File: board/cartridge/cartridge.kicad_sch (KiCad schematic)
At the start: 33 parts, among them J1 TF-115-BCP9, J2 KH-TYPE-C-16P, J3 TC2030-NL, P1 Card Edge, SW1 K3-1410S, SW2 K3-1410S, U1 AMS1117-3.3, U2 STM32G0B0RETx, U4 NAU8814Y, Y1 X322516MLB4SI

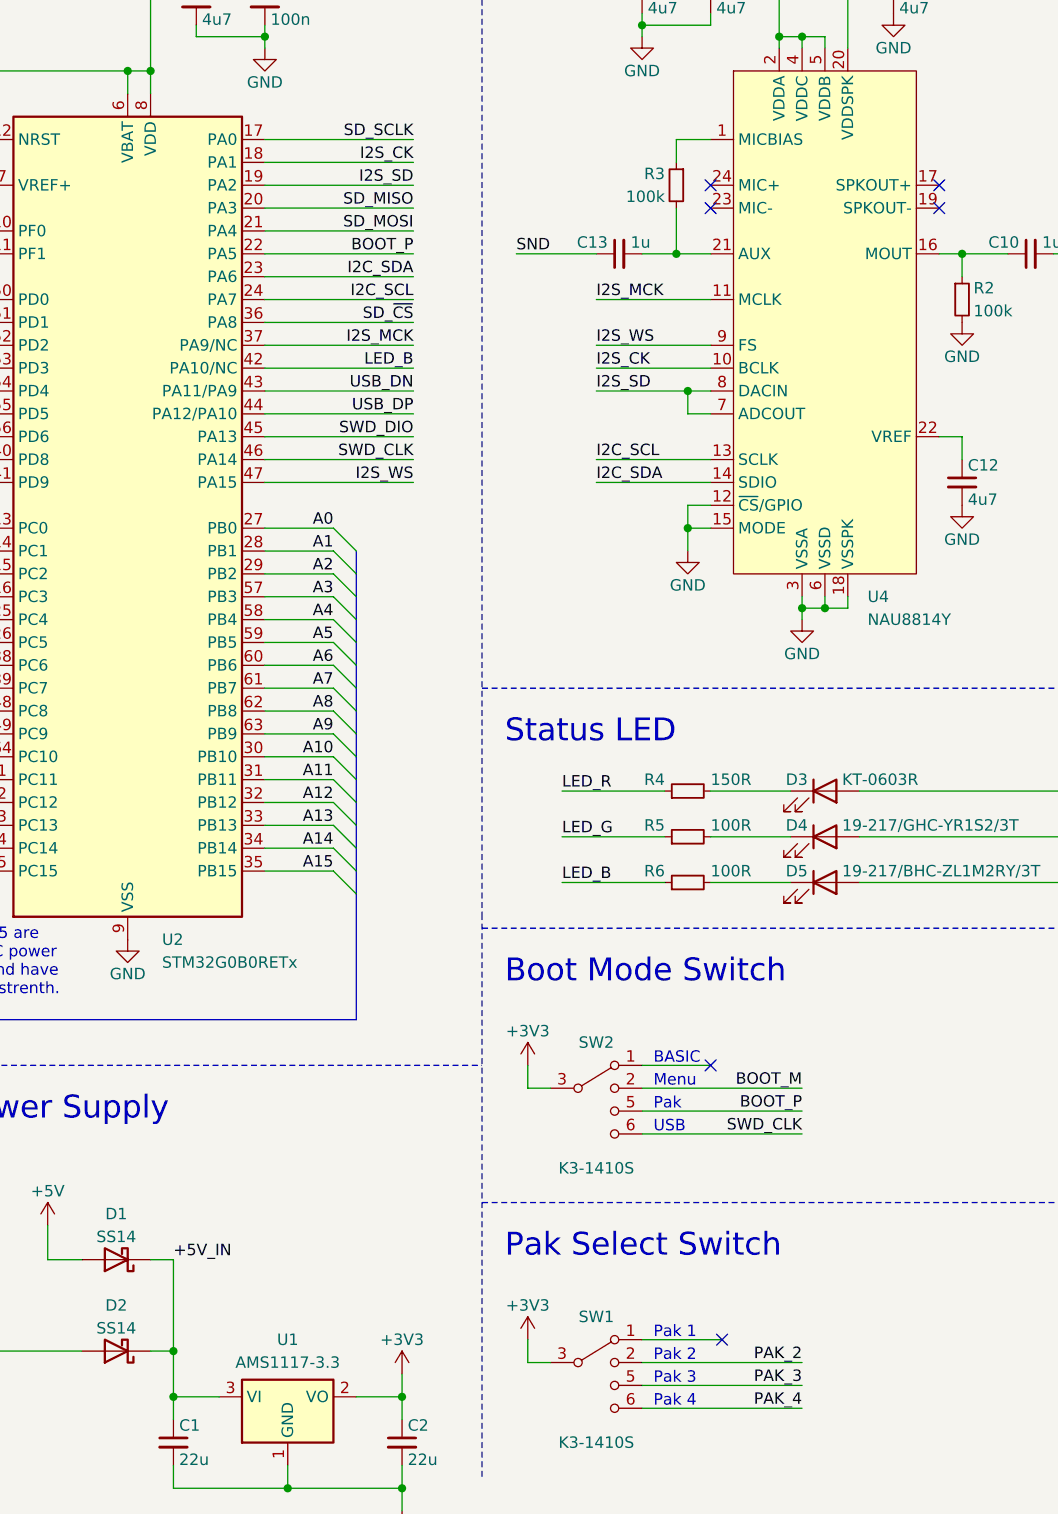
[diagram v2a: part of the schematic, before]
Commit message: Route power for the main ICs.
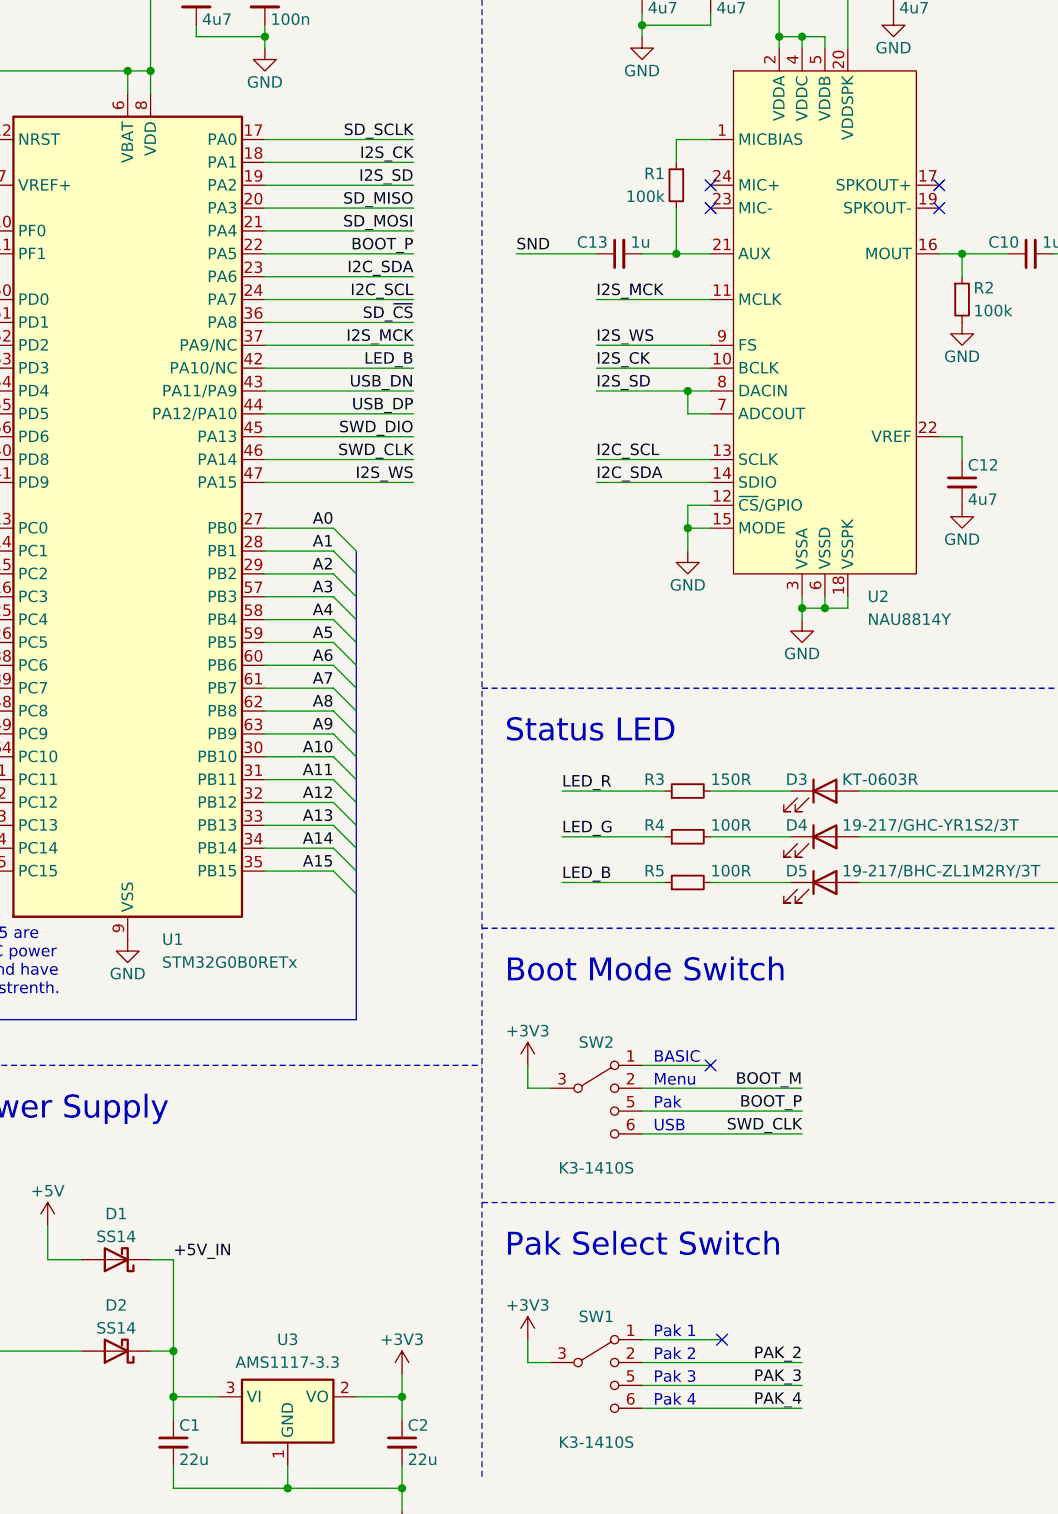
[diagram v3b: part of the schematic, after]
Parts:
- renumbered R3 to R1, R4 to R3, R5 to R4, R6 to R5, U2 to U1, U4 to U2, U1 to U3
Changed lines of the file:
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@@
   (symbol (lib_id "Device:R_Small") (at 215.9 125.73 90) (unit 1)
     (in_bom yes) (on_board yes) (dnp no)
-    (property "Reference" "R6" (at 213.36 124.46 90)
+    (property "Reference" "R5" (at 213.36 124.46 90)
       (effects (font (size 1.27 1.27)) (justify left))
     )
@@
       (project "cartridge"
         (path "/b6472d2e-e93c-4ee2-a887-2e70fff347c6"
-          (reference "R6") (unit 1)
+          (reference "R5") (unit 1)
         )
       )
@@
   (symbol (lib_id "Regulator_Linear:AMS1117-3.3") (at 171.45 182.88 0) (unit 1)
     (in_bom yes) (on_board yes) (dnp no) (fields_autoplaced)
-    (property "Reference" "U1" (at 171.45 176.53 0)
+    (property "Reference" "U3" (at 171.45 176.53 0)
       (effects (font (size 1.27 1.27)))
     )
@@
       (project "cartridge"
         (path "/b6472d2e-e93c-4ee2-a887-2e70fff347c6"
-          (reference "U1") (unit 1)
+          (reference "U3") (unit 1)
         )
       )
@@
   (symbol (lib_id "Device:R_Small") (at 215.9 120.65 90) (unit 1)
     (in_bom yes) (on_board yes) (dnp no)
-    (property "Reference" "R5" (at 213.36 119.38 90)
+    (property "Reference" "R4" (at 213.36 119.38 90)
       (effects (font (size 1.27 1.27)) (justify left))
     )
@@
       (project "cartridge"
         (path "/b6472d2e-e93c-4ee2-a887-2e70fff347c6"
-          (reference "R5") (unit 1)
+          (reference "R4") (unit 1)
         )
       )
@@
   (symbol (lib_id "MCU_ST_STM32G0:STM32G0B0RETx") (at 153.67 86.36 0) (unit 1)
     (in_bom yes) (on_board yes) (dnp no)
-    (property "Reference" "U2" (at 157.48 132.08 0)
+    (property "Reference" "U1" (at 157.48 132.08 0)
       (effects (font (size 1.27 1.27)) (justify left))
     )
@@
       (project "cartridge"
         (path "/b6472d2e-e93c-4ee2-a887-2e70fff347c6"
-          (reference "U2") (unit 1)
+          (reference "U1") (unit 1)
         )
       )
@@
   (symbol (lib_id "Device:R_Small") (at 215.9 115.57 90) (unit 1)
     (in_bom yes) (on_board yes) (dnp no)
-    (property "Reference" "R4" (at 213.36 114.3 90)
+    (property "Reference" "R3" (at 213.36 114.3 90)
       (effects (font (size 1.27 1.27)) (justify left))
     )
@@
       (project "cartridge"
         (path "/b6472d2e-e93c-4ee2-a887-2e70fff347c6"
-          (reference "R4") (unit 1)
+          (reference "R3") (unit 1)
         )
       )
@@
   (symbol (lib_id "Device:R_Small") (at 214.63 48.26 0) (mirror y) (unit 1)
     (in_bom yes) (on_board yes) (dnp no)
-    (property "Reference" "R3" (at 213.36 46.99 0)
+    (property "Reference" "R1" (at 213.36 46.99 0)
       (effects (font (size 1.27 1.27)) (justify left))
     )
@@
       (project "cartridge"
         (path "/b6472d2e-e93c-4ee2-a887-2e70fff347c6"
-          (reference "R3") (unit 1)
+          (reference "R1") (unit 1)
         )
       )
@@
   (symbol (lib_id "0Project:Nuvoton_NAU8814Y") (at 231.14 58.42 0) (unit 1)
     (in_bom yes) (on_board yes) (dnp no) (fields_autoplaced)
-    (property "Reference" "U4" (at 235.8741 93.98 0)
+    (property "Reference" "U2" (at 235.8741 93.98 0)
       (effects (font (size 1.27 1.27)) (justify left))
     )
@@
       (project "cartridge"
         (path "/b6472d2e-e93c-4ee2-a887-2e70fff347c6"
-          (reference "U4") (unit 1)
-        )
-      )
+          (reference "U2") (unit 1)
+        )
+      )

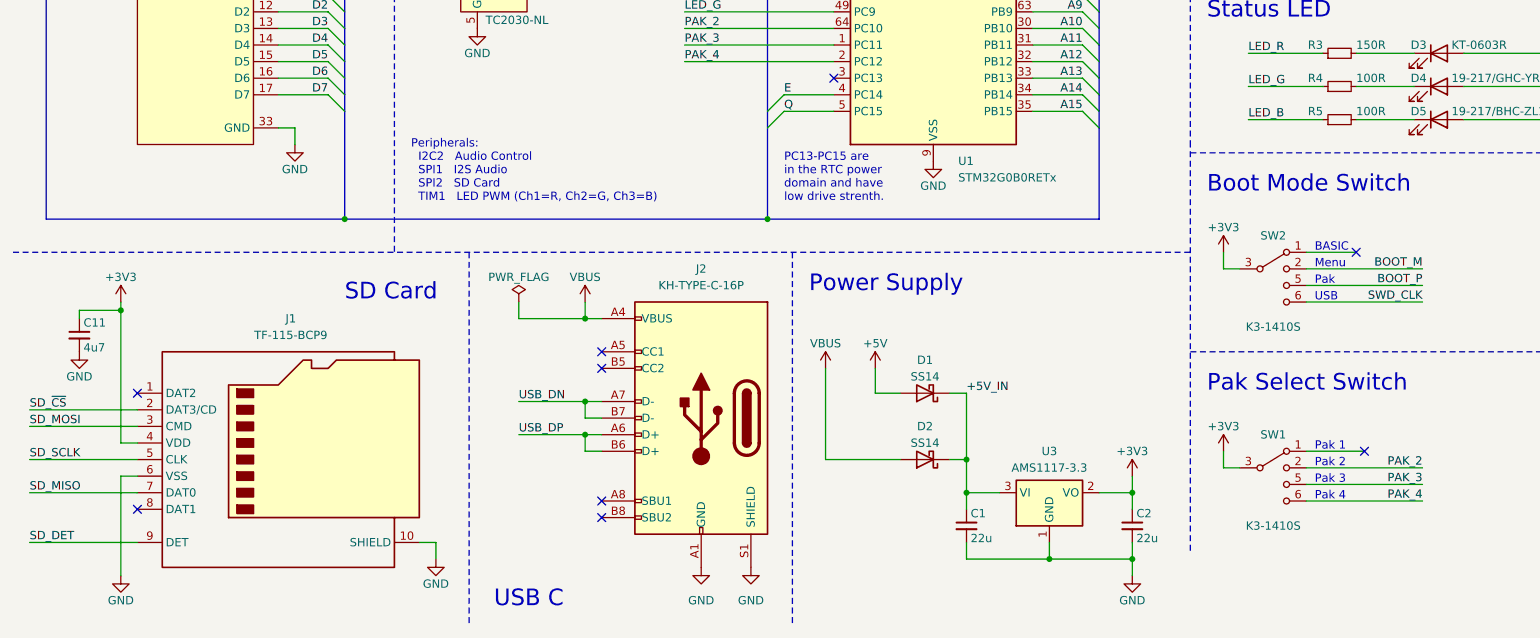
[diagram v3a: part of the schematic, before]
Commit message: Route everything else.
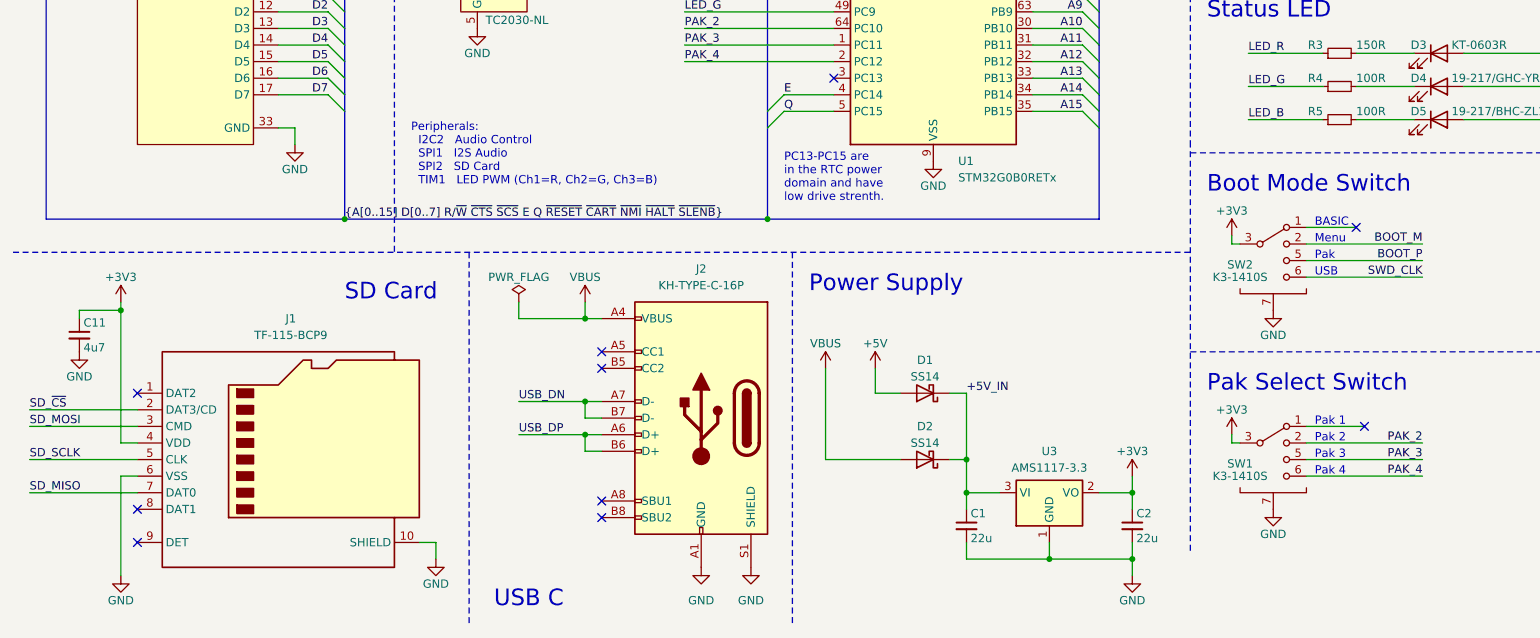
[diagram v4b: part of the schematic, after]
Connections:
- net GND: now also SW1.7 (SHIELD), SW2.7 (SHIELD)
- net SD_DET: no longer names the net of J1.9 (DET)
- no-connect marks 16 -> 17

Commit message: Misc board cleanup.
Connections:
- net VBUS: now also U1.3 (PC13)
- no-connect marks 17 -> 16
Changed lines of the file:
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@@
   (no_connect (at 93.98 106.68))
   (no_connect (at 243.84 48.26))
-  (no_connect (at 138.43 119.38))
   (bus_entry (at 60.96 116.84) (size 2.54 2.54)
     (stroke (width 0) (type default))
@@
     (stroke (width 0) (type default))
   )
+  (wire (pts (xy 109.22 115.57) (xy 109.22 119.38))
+    (stroke (width 0) (type default))
+  )
   (wire (pts (xy 130.81 86.36) (xy 138.43 86.36))
     (stroke (width 0) (type default))
@@
   )
   (wire (pts (xy 22.86 156.21) (xy 22.86 154.94))
+    (stroke (width 0) (type default))
+  )
+  (wire (pts (xy 138.43 119.38) (xy 109.22 119.38))
     (stroke (width 0) (type default))
   )
@@
         )
       )
+    )
+  )
+  (symbol (lib_id "power:VBUS") (at 109.22 115.57 0) (unit 1)
+    (in_bom yes) (on_board yes) (dnp no)
+    (property "Reference" "#PWR033" (at 109.22 119.38 0)
+      (effects (font (size 1.27 1.27)) hide)
+    )
+    (property "Value" "VBUS" (at 109.22 111.76 0)
+      (effects (font (size 1.27 1.27)))
+    )
+    (property "Footprint" "" (at 109.22 115.57 0)
+      (effects (font (size 1.27 1.27)) hide)
+    )
+    (property "Datasheet" "" (at 109.22 115.57 0)
+      (effects (font (size 1.27 1.27)) hide)
+    )
+    (pin "1")
+    (instances
+      (project "cartridge"
+        (path "/b6472d2e-e93c-4ee2-a887-2e70fff347c6"
+          (reference "#PWR033") (unit 1)
+        )
+      )

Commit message: Final cleanup for first cartridge prototype.
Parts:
- J2: value KH-TYPE-C-16P -> HC-TYPE-C-16P-01B; footprint 0Project:KH-TYPE-C-16P -> 0Project:HC-TYPE-C-16P-01B; LCSC C709357 -> C2894898
- R3: value 150R -> 220R
- R4: value 100R -> 120R
- R5: value 100R -> 150R
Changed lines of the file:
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@@
   (title_block
     (title "CoCo Chameleon - Cartridge Emulator")
-    (date "2023-11-24")
+    (date "2023-12-21")
     (rev "v0.1")
     (company "© 2023 Sam Hanes, licensed under CERN-OHL-W v2")
@@
   )
   (text "Peripherals:\n  I2C2   Audio Control\n  SPI1   I2S Audio\n  SPI2   SD Card\n  TIM1   LED PWM (Ch1=R, Ch2=G, Ch3=B)"
-    (at 73.66 135.89 0)
+    (at 73.66 133.35 0)
     (effects (font (size 1.27 1.27)) (justify left bottom))
   )
@@
       (effects (font (size 1.27 1.27)) (justify left))
     )
-    (property "Value" "100R" (at 218.44 124.46 90)
+    (property "Value" "150R" (at 218.44 124.46 90)
       (effects (font (size 1.27 1.27)) (justify right))
     )
@@
       (effects (font (size 1.27 1.27)) (justify left))
     )
-    (property "Value" "100R" (at 218.44 119.38 90)
+    (property "Value" "120R" (at 218.44 119.38 90)
       (effects (font (size 1.27 1.27)) (justify right))
     )
@@
       (effects (font (size 1.27 1.27)) (justify left))
     )
-    (property "Value" "150R" (at 218.44 114.3 90)
+    (property "Value" "220R" (at 218.44 114.3 90)
       (effects (font (size 1.27 1.27)) (justify right))
     )
@@
       (effects (font (size 1.27 1.27)))
     )
-    (property "Value" "KH-TYPE-C-16P" (at 118.11 151.13 0)
+    (property "Value" "HC-TYPE-C-16P-01B" (at 118.11 151.13 0)
       (effects (font (size 1.27 1.27)))
     )
-    (property "Footprint" "0Project:KH-TYPE-C-16P" (at 114.3 171.45 0)
+    (property "Footprint" "0Project:HC-TYPE-C-16P-01B" (at 114.3 171.45 0)
       (effects (font (size 1.27 1.27)) hide)
     )
-    (property "Datasheet" "https://datasheet.lcsc.com/lcsc/2009111434_Shenzhen-Kinghelm-Elec-KH-TYPE-C-16P_C709357.pdf" (at 114.3 171.45 0)
+    (property "Datasheet" "https://datasheet.lcsc.com/lcsc/2211161000_HCTL-HC-TYPE-C-16P-01B_C2894898.pdf" (at 114.3 171.45 0)
       (effects (font (size 1.27 1.27)) hide)
     )
-    (property "LCSC" "C709357" (at 118.11 171.45 0)
+    (property "LCSC" "C2894898" (at 118.11 171.45 0)
       (effects (font (size 1.27 1.27)) hide)
     )
